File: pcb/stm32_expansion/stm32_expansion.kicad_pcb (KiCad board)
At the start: 2 copper layers, 99.1 x 99.1 mm, 8 parts, among them J1 Conn_01x02_Male, P1 Conn_02x11_Odd_Even, P2 Conn_02x11_Odd_Even, P3 Conn_02x11_Odd_Even, P4 Conn_02x11_Odd_Even, P5 Conn_01x20_Female, P6 Conn_01x20_Female, U1 TJA1051T

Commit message: Update schematic.
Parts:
- moved P6 43.4 mm to (184.2, 116.8)
- moved P5 43.4 mm to (184.2, 101.6)
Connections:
- P5 pad 13: Net-(P5-Pad13) -> /Pin16
- P5 pad 14: Net-(P5-Pad14) -> /Pin17
- P5 pad 15: Net-(P5-Pad15) -> /Pin07
- P5 pad 16: Net-(P5-Pad16) -> /Pin08
- P6 pad 10: /Pin34 -> /Pin06
- P6 pad 11: /Pin35 -> /Pin05
- P6 pad 13: /Pin37 -> /Pin04
- P6 pad 14: /Pin38 -> /Pin03
- P6 pad 15: /Pin39 -> /Pin02
- P6 pad 16: /Pin40 -> /Pin01
- P6 pad 8: /Pin30 -> /Pin15
- P6 pad 9: /Pin33 -> /Pin14

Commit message: Update pcb.
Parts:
- removed U1: TJA1051T, Package_SO:SOIC-8_3.9x4.9mm_P1.27mm
- added Pad1: MountingHole_3mm_Pad, MountingHole:MountingHole_3mm_Pad, F.Cu at (94.0, 30.5)
- added Pad2: MountingHole_3mm_Pad, MountingHole:MountingHole_3mm_Pad, F.Cu at (185.4, 31.8)
- added Pad3: MountingHole_3mm_Pad, MountingHole:MountingHole_3mm_Pad, F.Cu at (94.0, 121.9)
- added Pad4: MountingHole_3mm_Pad, MountingHole:MountingHole_3mm_Pad, F.Cu at (185.4, 121.9)
- moved J1 116.3 mm to (175.3, 123.2), turned to 90 degrees
- moved P5 39.5 mm to (144.8, 99.1)
- moved P6 39.5 mm to (144.8, 114.3)
- moved P3 7.18 mm to (176.5, 74.9)
- moved P2 7.18 mm to (141.0, 85.1)
- moved P4 7.18 mm to (166.5, 39.4)
- moved P1 7.18 mm to (130.8, 49.5)
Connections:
- P6 pad 12: /Pin36 -> Net-(P6-Pad12)
- P6 pad 17: /Pin41 -> /Pin21
- P6 pad 18: /Pin42 -> /Pin20
- P6 pad 19: /Pin43 -> /Pin19
- P6 pad 20: /Pin44 -> /Pin18
- P6 pad 4: /Pin26 -> Net-(P6-Pad4)
- P6 pad 5: /Pin27 -> Net-(P6-Pad5)
- P6 pad 6: /Pin28 -> Net-(P6-Pad6)
- P6 pad 7: /Pin29 -> Net-(P6-Pad7)
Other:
- outline, holes or cut-outs redrawn

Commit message: Update pcb layout.
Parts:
- added C1: 0.1uF, Capacitor_Tantalum_SMD:CP_EIA-2012-12_Kemet-R, F.Cu at (175.6, 119.4)
- added C2: 30pF, Capacitor_Tantalum_SMD:CP_EIA-2012-12_Kemet-R, F.Cu at (170.6, 115.6)
- added C3: 30pF, Capacitor_Tantalum_SMD:CP_EIA-2012-12_Kemet-R, F.Cu at (170.6, 119.4)
- added CAN1: Conn_01x04, Connector_PinSocket_2.54mm:PinSocket_1x04_P2.54mm_Vertical, F.Cu at (118.1, 123.2)
- added Can2: Conn_01x02, Connector_PinSocket_2.54mm:PinSocket_1x02_P2.54mm_Vertical, F.Cu at (186.7, 110.5)
- added M1: Conn_01x05, Connector_PinSocket_2.54mm:PinSocket_1x05_P2.54mm_Vertical, F.Cu at (168.9, 29.2)
- added M2: Conn_01x05, Connector_PinSocket_2.54mm:PinSocket_1x05_P2.54mm_Vertical, F.Cu at (138.4, 29.2)
- added M3: Conn_01x05, Connector_PinSocket_2.54mm:PinSocket_1x05_P2.54mm_Vertical, F.Cu at (153.7, 29.2)
- added R1: 0R, Resistor_SMD:R_0805_2012Metric, F.Cu at (165.5, 115.6)
- added R2: 0R, Resistor_SMD:R_0805_2012Metric, F.Cu at (165.5, 119.4)
- added R3: 120R, Resistor_SMD:R_0805_2012Metric, F.Cu at (175.6, 115.6)
- added S1: Conn_01x03, Connector_PinSocket_2.54mm:PinSocket_1x03_P2.54mm_Vertical, F.Cu at (92.7, 36.8)
- added S2: Conn_01x03, Connector_PinSocket_2.54mm:PinSocket_1x03_P2.54mm_Vertical, F.Cu at (92.7, 47.0)
- added S3: Conn_01x03, Connector_PinSocket_2.54mm:PinSocket_1x03_P2.54mm_Vertical, F.Cu at (92.7, 57.1)
- added S4: Conn_01x03, Connector_PinSocket_2.54mm:PinSocket_1x03_P2.54mm_Vertical, F.Cu at (92.7, 67.3)
- added S5: Conn_01x03, Connector_PinSocket_2.54mm:PinSocket_1x03_P2.54mm_Vertical, F.Cu at (92.7, 77.5)
- added S6: Conn_01x03, Connector_PinSocket_2.54mm:PinSocket_1x03_P2.54mm_Vertical, F.Cu at (92.7, 87.6)
- added U1: TJA1051T, Package_SO:SOIC-8_3.9x4.9mm_P1.27mm, F.Cu at (156.2, 116.8)
- added UART1: Conn_01x04, Connector_PinSocket_2.54mm:PinSocket_1x04_P2.54mm_Vertical, F.Cu at (102.9, 123.2)
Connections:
- net /GND renamed GND
- P5 pad 7: Net-(P5-Pad7) -> /UART2_TX
- P5 pad 8: Net-(P5-Pad8) -> /UART2_RX
- P6 pad 4: Net-(P6-Pad4) -> /CAN_TX
- P6 pad 5: Net-(P6-Pad5) -> /CAN_RX

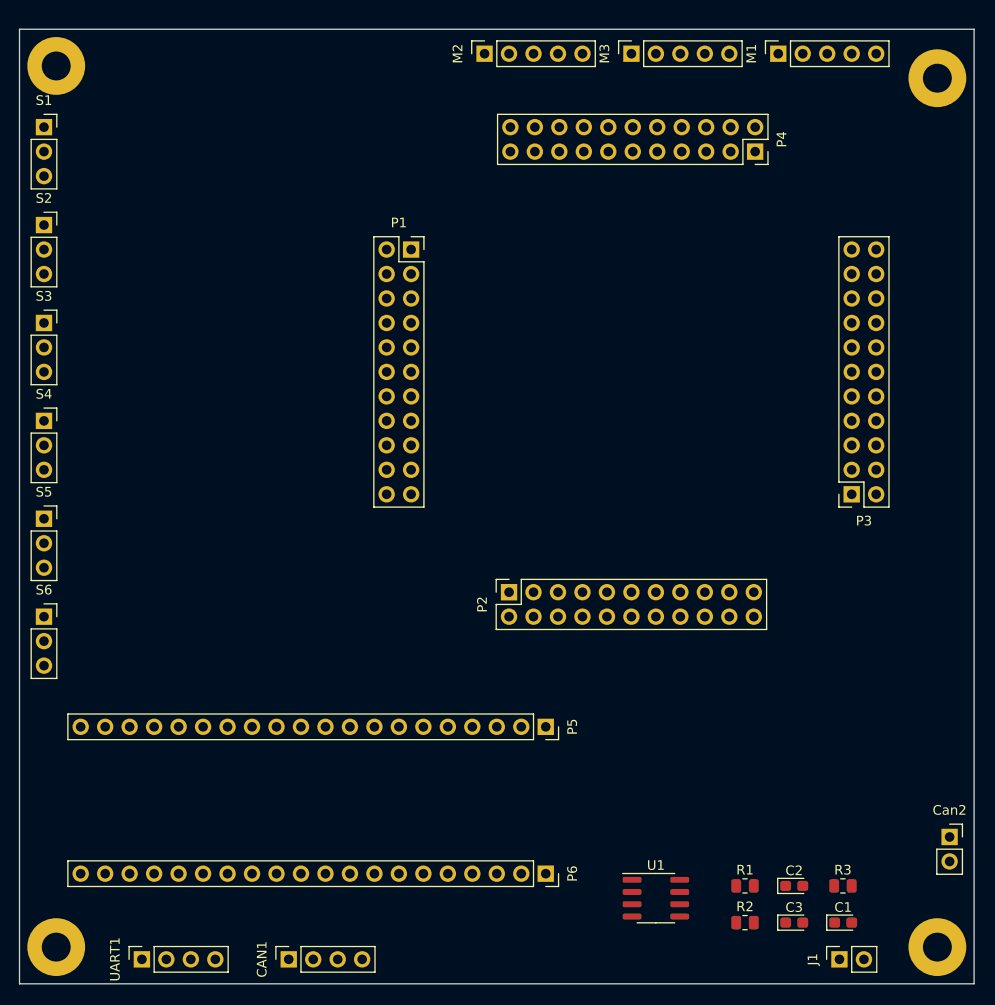
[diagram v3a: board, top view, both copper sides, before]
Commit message: update uart to lora.
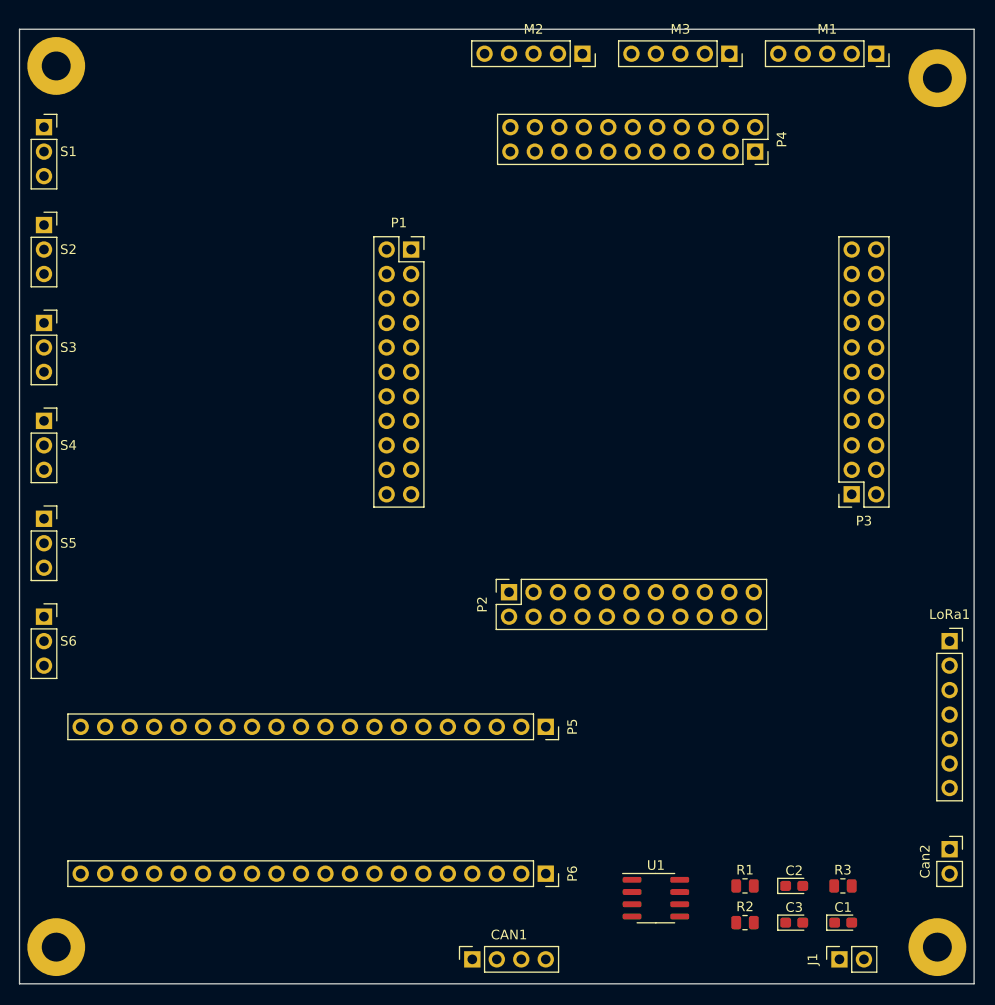
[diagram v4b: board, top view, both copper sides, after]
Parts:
- removed UART1: Conn_01x04, Connector_PinSocket_2.54mm:PinSocket_1x04_P2.54mm_Vertical
- added LoRa1: Conn_01x07, Connector_PinSocket_2.54mm:PinSocket_1x07_P2.54mm_Vertical, F.Cu at (186.7, 90.2)
- moved CAN1 19.0 mm to (137.2, 123.2)
- moved M3 10.2 mm to (163.8, 29.2), turned to 270 degrees
- moved M1 10.2 mm to (179.1, 29.2), turned to 270 degrees
- moved M2 10.2 mm to (148.6, 29.2), turned to 270 degrees
- moved Can2 1.27 mm to (186.7, 111.8)
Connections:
- P5 pad 4: Net-(P5-Pad4) -> /AUX
- P5 pad 5: Net-(P5-Pad5) -> /MD0
- P5 pad 6: Net-(P5-Pad6) -> /MD1

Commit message: complete pcb.
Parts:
- moved LoRa1 16.5 mm to (186.7, 106.7), turned to 180 degrees
- moved P5 2.54 mm to (147.3, 99.1)
- moved P6 2.54 mm to (147.3, 114.3)
- moved Pad2 1.27 mm to (185.4, 30.5)
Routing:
- net GND: track 0.00 -> 391.1 mm
- net /5V: track 0.00 -> 222.3 mm
- net /Pin01: track 0.00 -> 82.4 mm
- net /Pin97: track 0.00 -> 81.4 mm
- net /Pin03: track 0.00 -> 80.3 mm
- net /Pin91: track 0.00 -> 78.6 mm
- net /Pin02: track 0.00 -> 76.8 mm
- net /Pin95: track 0.00 -> 75.1 mm
- net /Pin04: track 0.00 -> 74.3 mm
- net /Pin96: track 0.00 -> 73.2 mm
- net /Pin06: track 0.00 -> 72.6 mm
- net /Pin19: track 0.00 -> 68.3 mm
- net /Pin14: track 0.00 -> 66.7 mm
- net /Pin92: track 0.00 -> 66.5 mm
- net /Pin05: track 0.00 -> 65.9 mm
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- added copper zone on B.Cu, net GND
- added copper zone on F.Cu, net GND
